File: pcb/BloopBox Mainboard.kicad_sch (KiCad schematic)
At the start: 47 parts, among them J1 SPKR, J2 Raspberry_Pi, J3 I2C, J4 TailBoard, J5 GPIO, J6 NFCModuleV3, J7 ExtLED, Q1 2N7002, Q2 2N7002, Q3 2N7002, Q4 2N7002, Q5 2N7002, Q6 2N7002, U1 MAX98357

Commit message: feat: prepare files for automatic version numbering
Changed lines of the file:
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@@
   (title_block
     (title "BloopBox Mainboard")
-    (date "2022-12-01")
-    (rev "1.0")
+    (date "${DATE}")
+    (rev "${VERSION}")
     (company "Qetesh")
   )
@@
     (pin "2")
   )
-  (symbol (lib_id "power:PWR_FLAG") (at -29.21 182.88 180) (unit 1)
-    (in_bom yes) (on_board yes) (fields_autoplaced)
-    (property "Reference" "#FLG01" (id 0) (at -29.21 184.785 0)
-      (effects (font (size 1.27 1.27)) hide)
-    )
-    (property "Value" "PWR_FLAG" (id 1) (at -30.8609 184.5838 0)
-      (effects (font (size 1.27 1.27)) (justify left))
-    )
-    (property "Footprint" "" (id 2) (at -29.21 182.88 0)
-      (effects (font (size 1.27 1.27)) hide)
-    )
-    (property "Datasheet" "~" (id 3) (at -29.21 182.88 0)
+  (symbol (lib_id "power:PWR_FLAG") (at -31.75 182.88 180) (unit 1)
+    (in_bom yes) (on_board yes) (fields_autoplaced)
+    (property "Reference" "#FLG01" (id 0) (at -31.75 184.785 0)
+      (effects (font (size 1.27 1.27)) hide)
+    )
+    (property "Value" "PWR_FLAG" (id 1) (at -33.4009 184.5838 0)
+      (effects (font (size 1.27 1.27)) (justify left))
+    )
+    (property "Footprint" "" (id 2) (at -31.75 182.88 0)
+      (effects (font (size 1.27 1.27)) hide)
+    )
+    (property "Datasheet" "~" (id 3) (at -31.75 182.88 0)
       (effects (font (size 1.27 1.27)) hide)
     )
@@
     (pin "1")
   )
-  (symbol (lib_id "power:+5V") (at -29.21 182.88 0) (unit 1)
-    (in_bom yes) (on_board yes) (fields_autoplaced)
-    (property "Reference" "#PWR016" (id 0) (at -29.21 186.69 0)
-      (effects (font (size 1.27 1.27)) hide)
-    )
-    (property "Value" "+5V" (id 1) (at -30.6069 182.0438 0)
-      (effects (font (size 1.27 1.27)) (justify right))
-    )
-    (property "Footprint" "" (id 2) (at -29.21 182.88 0)
-      (effects (font (size 1.27 1.27)) hide)
-    )
-    (property "Datasheet" "" (id 3) (at -29.21 182.88 0)
-      (effects (font (size 1.27 1.27)) hide)
-    )
+  (symbol (lib_id "power:+5V") (at -31.75 182.88 0) (unit 1)
+    (in_bom yes) (on_board yes) (fields_autoplaced)
+    (property "Reference" "#PWR016" (id 0) (at -31.75 186.69 0)
+      (effects (font (size 1.27 1.27)) hide)
+    )
+    (property "Value" "+5V" (id 1) (at -31.75 179.3042 0))
+    (property "Footprint" "" (id 2) (at -31.75 182.88 0)
+      (effects (font (size 1.27 1.27)) hide)
+    )
+    (property "Datasheet" "" (id 3) (at -31.75 182.88 0)
+      (effects (font (size 1.27 1.27)) hide)
+    )

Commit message: feat: add UART to GPIO-Header
Adding the UART TX and RX pins to the GPIO header for debugging console access
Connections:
- net +3V3: now also J5.5 (Pin_5); no longer J5.6 (Pin_6)
- net GND: now also J5.6 (Pin_6); no longer J5.5 (Pin_5)
- net RX: now reaches J2.10 (GPIO15/RXD)
- net RX: now also J5.2 (Pin_2)
- net TX: now reaches J2.8 (GPIO14/TXD)
- net TX: now also J5.4 (Pin_4)
- net GPIO1: no longer names the net of J2.22 (GPIO25)
- net GPIO1: no longer J5.1 (Pin_1)
- net GPIO2 renamed GPIO5
- net GPIO5: now also J5.1 (Pin_1); no longer J5.2 (Pin_2)
- net GPIO3 renamed GPIO6
- net GPIO4: no longer names the net of J2.32 (PWM0/GPIO12)
- net GPIO4: no longer J5.4 (Pin_4)
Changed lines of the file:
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@@
   (no_connect (at 73.66 63.5))
   (no_connect (at 73.66 53.34))
-  (no_connect (at 33.02 38.1))
-  (no_connect (at 33.02 40.64))
+  (no_connect (at 33.02 73.66))
+  (no_connect (at 73.66 78.74))
   (no_connect (at 73.66 40.64))
   (no_connect (at 73.66 38.1))
@@
     (effects (font (size 1.27 1.27)) (justify left bottom))
   )
-  (label "GPIO4" (at 260.35 129.54 0)
-    (effects (font (size 1.27 1.27)) (justify left bottom))
-  )
   (label "SDA" (at 73.66 45.72 0)
     (effects (font (size 1.27 1.27)) (justify left bottom))
@@
     (effects (font (size 1.27 1.27)) (justify right bottom))
   )
-  (label "GPIO1" (at 247.65 127 180)
+  (label "TX" (at 33.02 38.1 180)
+    (effects (font (size 1.27 1.27)) (justify right bottom))
+  )
+  (label "GPIO5" (at 247.65 127 180)
     (effects (font (size 1.27 1.27)) (justify right bottom))
   )
@@
     (effects (font (size 1.27 1.27)) (justify right bottom))
   )
+  (label "RX" (at 260.35 127 0)
+    (effects (font (size 1.27 1.27)) (justify left bottom))
+  )
   (label "LED_PWM" (at 113.03 90.17 180)
     (effects (font (size 1.27 1.27)) (justify right bottom))
@@
     (effects (font (size 1.27 1.27)) (justify right bottom))
   )
-  (label "GPIO1" (at 33.02 73.66 180)
-    (effects (font (size 1.27 1.27)) (justify right bottom))
+  (label "GPIO5" (at 73.66 55.88 0)
+    (effects (font (size 1.27 1.27)) (justify left bottom))
   )
   (label "AMP_LRCLK" (at 204.47 43.18 180)
@@
     (effects (font (size 1.27 1.27)) (justify right bottom))
   )
-  (label "GPIO4" (at 73.66 78.74 0)
-    (effects (font (size 1.27 1.27)) (justify left bottom))
-  )
   (label "NFC-Select" (at 204.47 128.27 180)
     (effects (font (size 1.27 1.27)) (justify right bottom))
@@
     (effects (font (size 1.27 1.27)) (justify right bottom))
   )
+  (label "RX" (at 33.02 40.64 180)
+    (effects (font (size 1.27 1.27)) (justify right bottom))
+  )
   (label "V_I2C" (at 144.78 116.84 90)
     (effects (font (size 1.27 1.27)) (justify left bottom))
@@
     (effects (font (size 1.27 1.27)) (justify right bottom))
   )
-  (label "GPIO2" (at 73.66 55.88 0)
+  (label "GPIO6" (at 73.66 58.42 0)
     (effects (font (size 1.27 1.27)) (justify left bottom))
   )
@@
     (effects (font (size 1.27 1.27)) (justify left bottom))
   )
+  (label "TX" (at 260.35 129.54 0)
+    (effects (font (size 1.27 1.27)) (justify left bottom))
+  )
   (label "Rg" (at 133.35 54.61 0)
     (effects (font (size 1.27 1.27)) (justify left bottom))
   )
-  (label "GPIO2" (at 260.35 127 0)
-    (effects (font (size 1.27 1.27)) (justify left bottom))
+  (label "GPIO6" (at 247.65 129.54 180)
+    (effects (font (size 1.27 1.27)) (justify right bottom))
   )
   (label "Tail7" (at 62.23 143.51 180)
@@
     (effects (font (size 1.27 1.27)) (justify left bottom))
   )
-  (label "GPIO3" (at 73.66 58.42 0)
-    (effects (font (size 1.27 1.27)) (justify left bottom))
-  )
   (label "Button2" (at 31.75 146.05 180)
     (effects (font (size 1.27 1.27)) (justify right bottom))
   )
   (label "V_I2C" (at 166.37 124.46 180)
-    (effects (font (size 1.27 1.27)) (justify right bottom))
-  )
-  (label "GPIO3" (at 247.65 129.54 180)
     (effects (font (size 1.27 1.27)) (justify right bottom))
   )
@@
     (pin "3")
   )
-  (symbol (lib_id "power:GND") (at 247.65 132.08 270) (unit 1)
-    (in_bom yes) (on_board yes) (fields_autoplaced)
-    (property "Reference" "#PWR033" (id 0) (at 241.3 132.08 0)
-      (effects (font (size 1.27 1.27)) hide)
-    )
-    (property "Value" "GND" (id 1) (at 244.4751 132.5138 90)
+  (symbol (lib_id "power:GND") (at 260.35 132.08 90) (unit 1)
+    (in_bom yes) (on_board yes) (fields_autoplaced)
+    (property "Reference" "#PWR033" (id 0) (at 266.7 132.08 0)
+      (effects (font (size 1.27 1.27)) hide)
+    )
+    (property "Value" "GND" (id 1) (at 263.525 132.5138 90)
       (effects (font (size 1.27 1.27)) (justify right))
     )
-    (property "Footprint" "" (id 2) (at 247.65 132.08 0)
-      (effects (font (size 1.27 1.27)) hide)
-    )
-    (property "Datasheet" "" (id 3) (at 247.65 132.08 0)
+    (property "Footprint" "" (id 2) (at 260.35 132.08 0)
+      (effects (font (size 1.27 1.27)) hide)
+    )
+    (property "Datasheet" "" (id 3) (at 260.35 132.08 0)
       (effects (font (size 1.27 1.27)) hide)
     )
@@
     (pin "1")
   )
-  (symbol (lib_id "power:+3V3") (at 260.35 132.08 270) (unit 1)
-    (in_bom yes) (on_board yes) (fields_autoplaced)
-    (property "Reference" "#PWR030" (id 0) (at 256.54 132.08 0)
-      (effects (font (size 1.27 1.27)) hide)
-    )
-    (property "Value" "+3V3" (id 1) (at 263.525 132.5138 90)
-      (effects (font (size 1.27 1.27)) (justify left))
-    )
-    (property "Footprint" "" (id 2) (at 260.35 132.08 0)
-      (effects (font (size 1.27 1.27)) hide)
-    )
-    (property "Datasheet" "" (id 3) (at 260.35 132.08 0)
-      (effects (font (size 1.27 1.27)) hide)
-    )
+  (symbol (lib_id "power:+3V3") (at 247.65 132.08 90) (unit 1)
+    (in_bom yes) (on_board yes) (fields_autoplaced)
+    (property "Reference" "#PWR030" (id 0) (at 251.46 132.08 0)
+      (effects (font (size 1.27 1.27)) hide)
+    )
+    (property "Value" "+3V3" (id 1) (at 244.475 132.5138 90)
+      (effects (font (size 1.27 1.27)) (justify left))
+    )
+    (property "Footprint" "" (id 2) (at 247.65 132.08 0)
+      (effects (font (size 1.27 1.27)) hide)
+    )
+    (property "Datasheet" "" (id 3) (at 247.65 132.08 0)
+      (effects (font (size 1.27 1.27)) hide)
+    )

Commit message: fix: remove Tailboard IO protection resistors
After removing the PD controller from the tailboard, the LEDs are directly connected to the mainboard so the protection resistors had to go
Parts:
- removed R21, R22: 1k, Resistor_SMD:R_0402_1005Metric, symbol Device:R_Small
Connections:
- net Tail2 is gone; now on net Tail_IO1: J4.2 (Pin_2)
- net Tail7 is gone; now on net Tail_IO2: J4.7 (Pin_7)
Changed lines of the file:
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@@
-    (stroke (width 0) (type default) (color 0 0 0 0))
-  )
-  (wire (pts (xy 41.91 130.81) (xy 62.23 130.81))
     (stroke (width 0) (type default) (color 0 0 0 0))
   )
@@
     (stroke (width 0) (type default) (color 0 0 0 0))
   )
-  (wire (pts (xy 31.75 130.81) (xy 36.83 130.81))
+  (wire (pts (xy 31.75 130.81) (xy 62.23 130.81))
     (stroke (width 0) (type default) (color 0 0 0 0))
   )
@@
     (stroke (width 0) (type default) (color 0 0 0 0))
   )
-  (wire (pts (xy 41.91 143.51) (xy 62.23 143.51))
+  (wire (pts (xy 31.75 143.51) (xy 62.23 143.51))
     (stroke (width 0) (type default) (color 0 0 0 0))
   )
@@
   )
   (polyline (pts (xy 19.05 106.68) (xy 78.74 106.68))
-    (stroke (width 0) (type default) (color 0 0 0 0))
-  )
-  (wire (pts (xy 31.75 143.51) (xy 36.83 143.51))
     (stroke (width 0) (type default) (color 0 0 0 0))
   )
@@
     (effects (font (size 1.27 1.27)) (justify left bottom))
   )
-  (label "Tail2" (at 62.23 130.81 180)
-    (effects (font (size 1.27 1.27)) (justify right bottom))
-  )
   (label "Rc" (at 143.51 38.1 0)
     (effects (font (size 1.27 1.27)) (justify left bottom))
@@
   )
   (label "GPIO6" (at 247.65 129.54 180)
-    (effects (font (size 1.27 1.27)) (justify right bottom))
-  )
-  (label "Tail7" (at 62.23 143.51 180)
     (effects (font (size 1.27 1.27)) (justify right bottom))
   )
@@
     (pin "3")
   )
-  (symbol (lib_id "Device:R_Small") (at 39.37 130.81 90) (unit 1)
-    (in_bom yes) (on_board yes) (fields_autoplaced)
-    (property "Reference" "R21" (id 0) (at 39.37 133.577 90))
-    (property "Value" "1k" (id 1) (at 39.37 136.1139 90))
-    (property "Footprint" "Resistor_SMD:R_0402_1005Metric" (id 2) (at 39.37 130.81 0)
-      (effects (font (size 1.27 1.27)) hide)
-    )
-    (property "Datasheet" "~" (id 3) (at 39.37 130.81 0)
-      (effects (font (size 1.27 1.27)) hide)
-    )
-    (pin "1")
-    (pin "2")
-  )
   (symbol (lib_id "Device:R_Small") (at 130.81 64.77 270) (unit 1)
     (in_bom yes) (on_board yes) (fields_autoplaced)
@@
     )
     (property "LCSC" "C25794" (id 4) (at 96.52 124.46 0)
-      (effects (font (size 1.27 1.27)) hide)
-    )
-    (pin "1")
-    (pin "2")
-  )
-  (symbol (lib_id "Device:R_Small") (at 39.37 143.51 90) (unit 1)
-    (in_bom yes) (on_board yes) (fields_autoplaced)
-    (property "Reference" "R22" (id 0) (at 39.37 139.0736 90))
-    (property "Value" "1k" (id 1) (at 39.37 141.6105 90))
-    (property "Footprint" "Resistor_SMD:R_0402_1005Metric" (id 2) (at 39.37 143.51 0)
-      (effects (font (size 1.27 1.27)) hide)
-    )
-    (property "Datasheet" "~" (id 3) (at 39.37 143.51 0)
       (effects (font (size 1.27 1.27)) hide)
     )
@@
       (reference "R20") (unit 1) (value "1k") (footprint "Resistor_SMD:R_0402_1005Metric")
     )
-    (path "/5d781359-2cd1-4802-918c-3cc1a5c9aef5"
-      (reference "R21") (unit 1) (value "1k") (footprint "Resistor_SMD:R_0402_1005Metric")
-    )
-    (path "/703397b4-6f36-474d-96b5-87ba3d179938"
-      (reference "R22") (unit 1) (value "1k") (footprint "Resistor_SMD:R_0402_1005Metric")
-    )
     (path "/5a4e233f-cc72-418b-9d26-582c33f6682f"

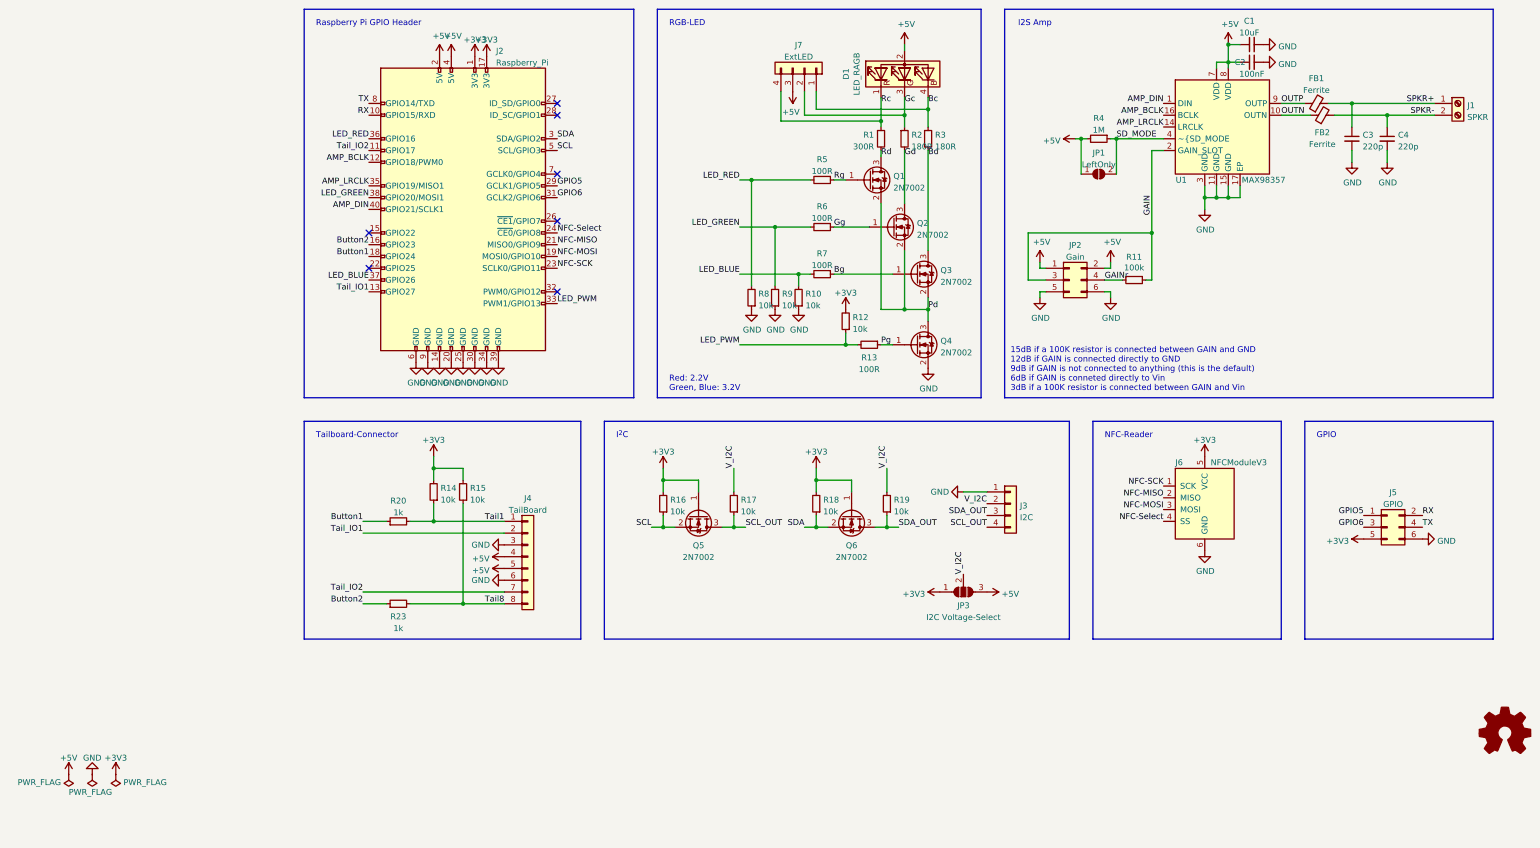
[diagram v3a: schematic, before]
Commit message: feat!: change NFC connector to RC522 pinout
Switch the NFC-connector from the PN532 module to the RC522 since the PN532 works not reliable with NTAG
Connect IRQ and RST lines while doing so
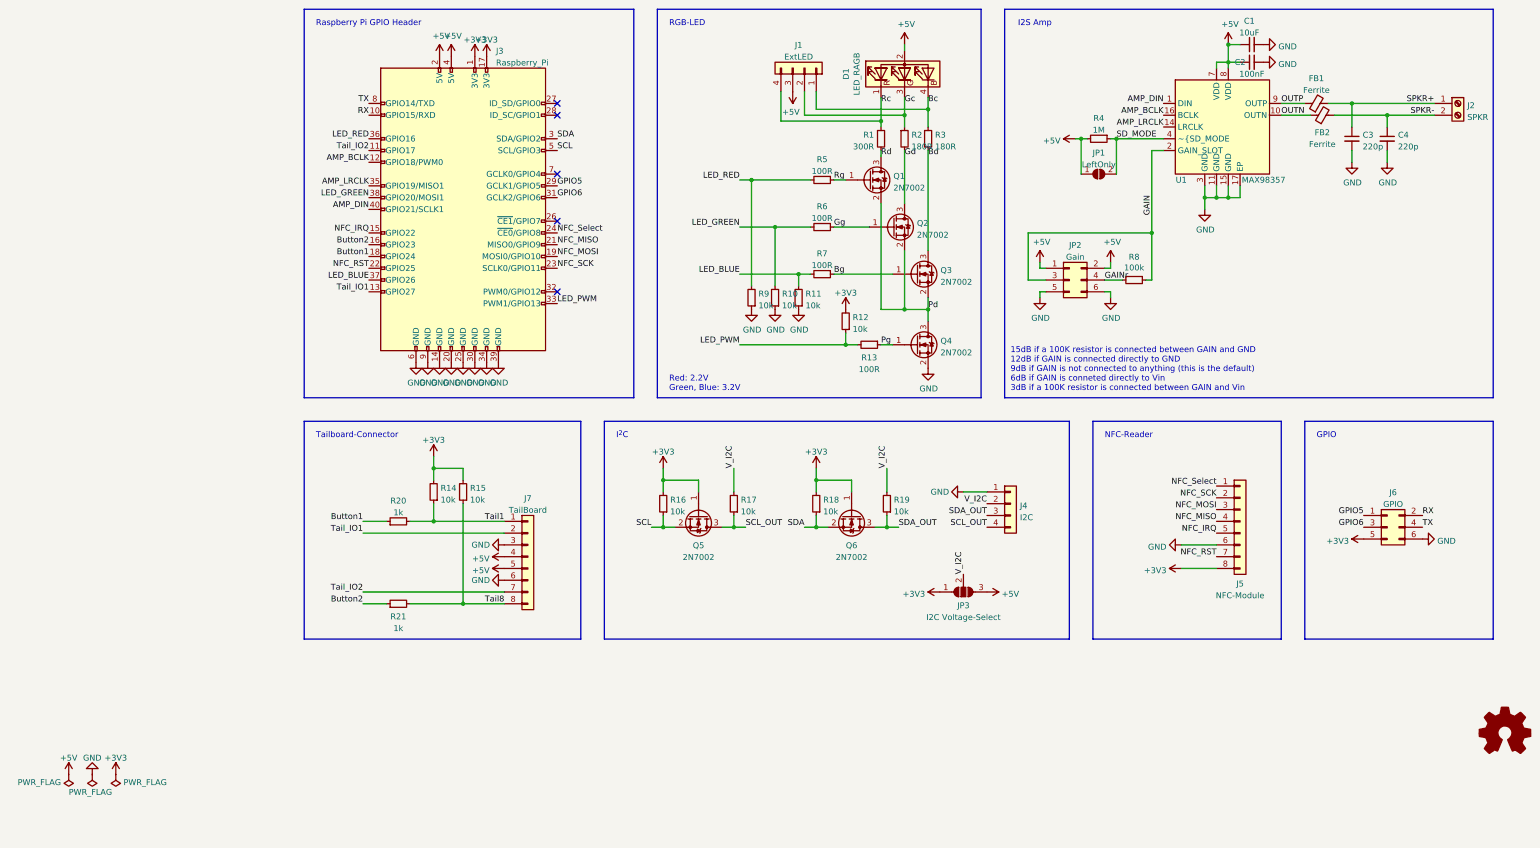
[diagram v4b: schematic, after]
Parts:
- removed J6: NFCModuleV3, Connector_JST:JST_PH_S6B-PH-K_1x06_P2.00mm_Horizontal, symbol My_Symbols:NFCModuleV3-RF_Module
- added J5: NFC-Module, Connector_JST:JST_PH_S8B-PH-K_1x08_P2.00mm_Horizontal, symbol Connector_Generic:Conn_01x08
- renumbered J7 to J1, J1 to J2, J2 to J3, J3 to J4, J5 to J6, J4 to J7, R9 to R10, R10 to R11, R23 to R21, R11 to R8, R8 to R9
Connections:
- net +3V3: now also J5.8 (Pin_8)
- net GND: now also J5.6 (Pin_6)
- net NFC_IRQ: now reaches J3.15 (GPIO22)
- net NFC_IRQ: now also J5.5 (Pin_5)
- net NFC_RST: now reaches J3.22 (GPIO25)
- net NFC_RST: now also J5.7 (Pin_7)
- net NFC-MISO renamed NFC_MISO
- net NFC_MISO: now also J5.4 (Pin_4)
- net NFC-MOSI renamed NFC_MOSI
- net NFC_MOSI: now also J5.3 (Pin_3)
- net NFC-SCK renamed NFC_SCK
- net NFC_SCK: now also J5.2 (Pin_2)
- net NFC-Select renamed NFC_Select
- net NFC_Select: now also J5.1 (Pin_1)
- no-connect marks 7 -> 5

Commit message: feat: add ID EEPROM
Add (optional) ID EEPROM to the board that will allow some of the hardware to be auto-configured on the Raspberry Pi.
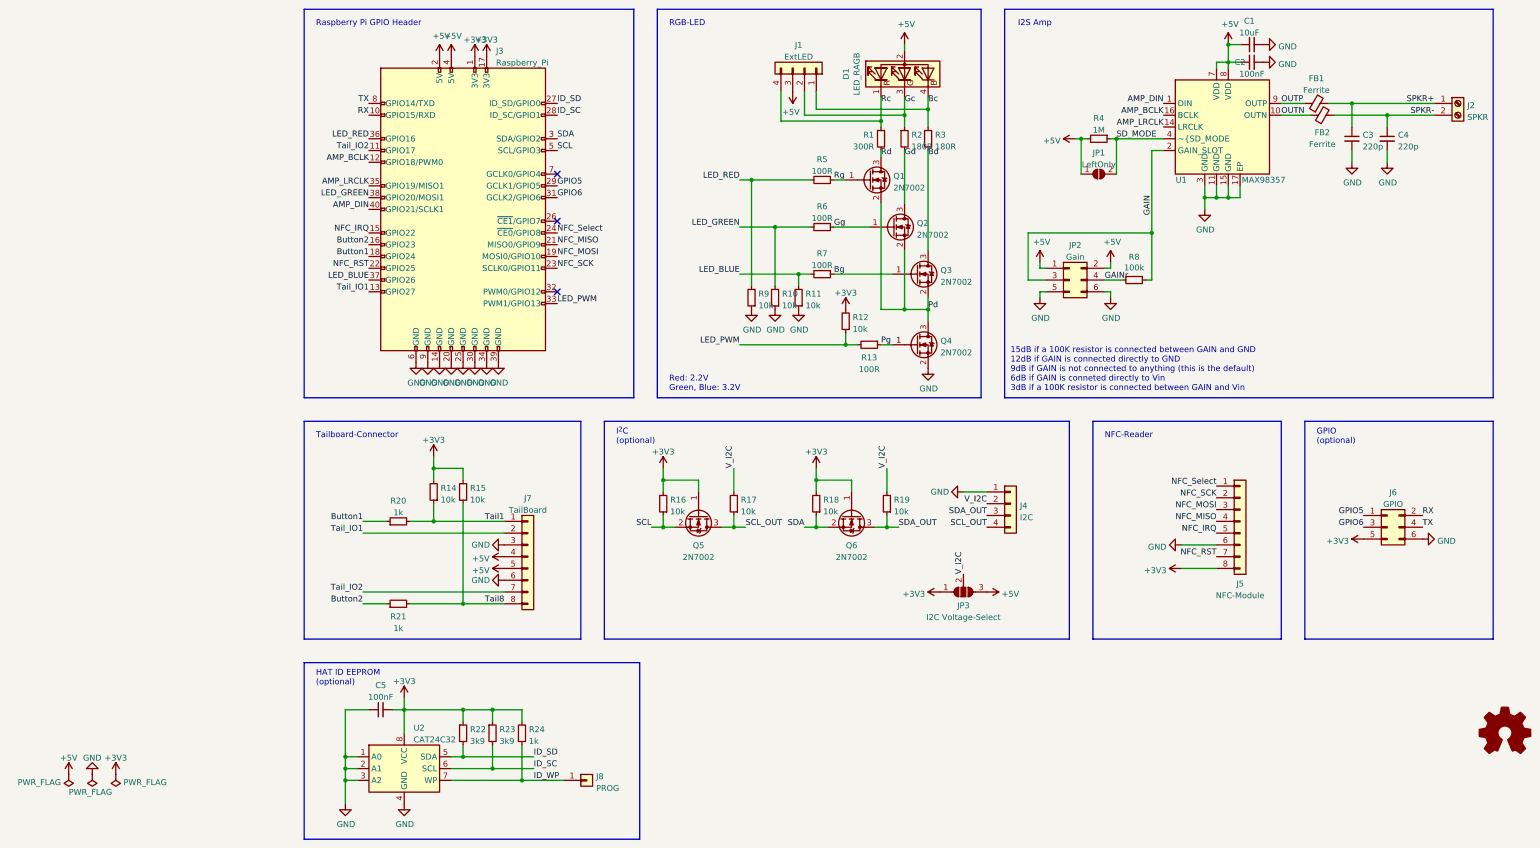
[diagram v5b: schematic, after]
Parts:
- added C5: 100nF, Capacitor_SMD:C_0402_1005Metric, symbol Device:C_Small
- added J8: PROG, TestPoint:TestPoint_THTPad_1.0x1.0mm_Drill0.5mm, symbol Connector_Generic:Conn_01x01
- added R22, R23: 3k9, Resistor_SMD:R_0402_1005Metric, symbol Device:R_Small
- added R24: 1k, Resistor_SMD:R_0402_1005Metric, symbol Device:R_Small
- added U2: CAT24C32, Package_DFN_QFN:DFN-8-1EP_3x2mm_P0.5mm_EP1.3x1.5mm, symbol Memory_EEPROM:CAT24C128
- J1: LCSC (none) -> C722777
- J6: LCSC (none) -> C239334
- JP2: footprint Connector_PinHeader_1.27mm:PinHeader_2x03_P1.27mm_Vertical -> Connector_PinHeader_2.00mm:PinHeader_2x03_P2.00mm_Vertical; LCSC (none) -> C225288
- R10, R11, R12, R14, R15, R16, R17, R18, R19, R9: LCSC C25794 -> C25744
- R20, R21: LCSC (none) -> C11702
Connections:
- net +3V3: now also C5.2, R22.1, R23.1, R24.2, U2.8 (VCC)
- net GND: now also C5.1, U2.1 (A0), U2.2 (A1), U2.3 (A2), U2.4 (GND)
- net ID_SD: now reaches J3.27 (ID_SD/GPIO0)
- net ID_SD: now also R22.2, U2.5 (SDA)
- net ID_SC: now reaches J3.28 (ID_SC/GPIO1)
- net ID_SC: now also R23.2, U2.6 (SCL)
- new net ID_WP: J8.1 (Pin_1), R24.1, U2.7 (WP)
- no-connect marks 5 -> 3
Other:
- note added: "GPIO (optional)"
- note added: "HAT ID EEPROM (optional)"
- note added: "I^{2}C (optional)"
- note removed: "GPIO"
- note removed: "I^{2}C"
